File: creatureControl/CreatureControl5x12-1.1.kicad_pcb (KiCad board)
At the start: 2 copper layers, 120 x 50 mm, 42 parts, among them J1 USB_C_Receptacle_GCT_USB4125-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, J2 BarrelJack_Horizontal, J3 TerminalBlock_4Ucon_1x02_P3.5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

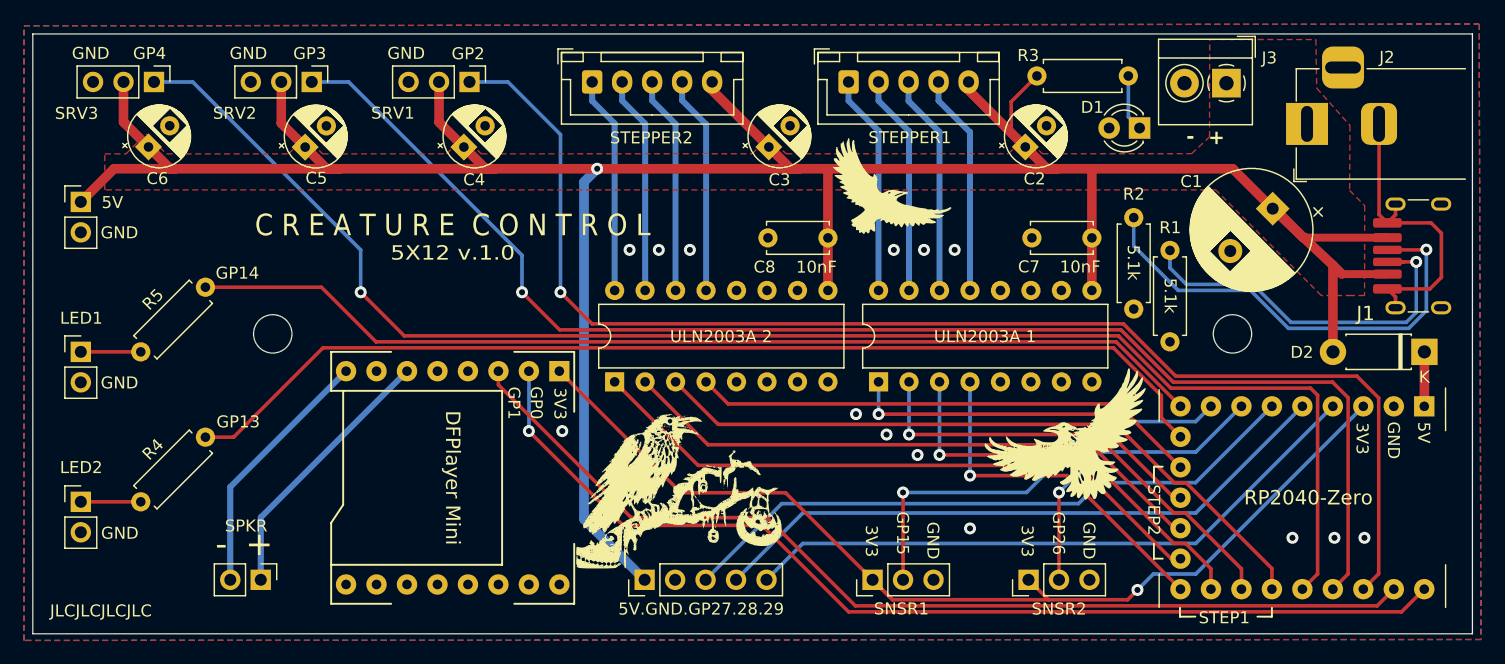
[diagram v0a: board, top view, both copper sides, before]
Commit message: Update CC5x12 to v1.1
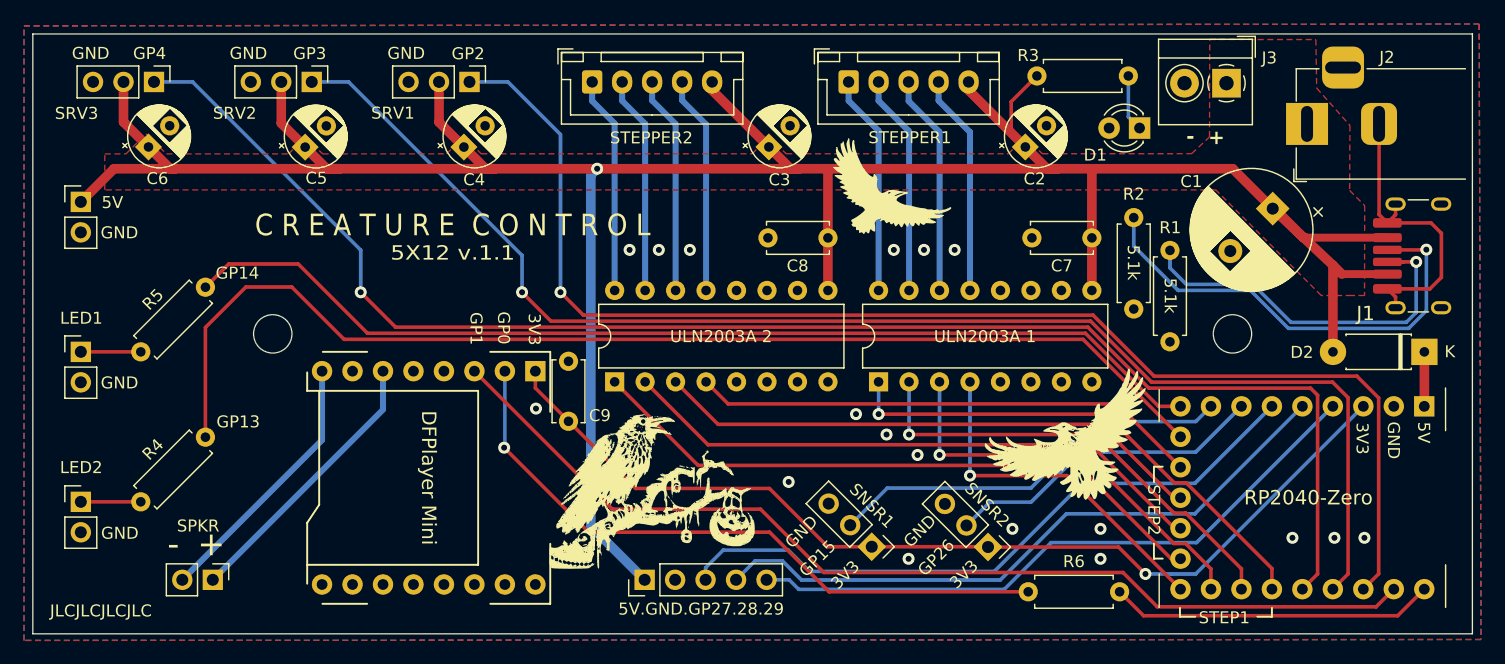
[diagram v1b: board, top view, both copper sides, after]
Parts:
- added C9: C_Disc_D5.0mm_W2.5mm_P5.00mm, Capacitor_THT:C_Disc_D5.0mm_W2.5mm_P5.00mm, F.Cu at (124.7, 62.3)
- added R6: 5.1 kΩ, Resistor_THT:R_Axial_DIN0207_L6.3mm_D2.5mm_P7.62mm_Horizontal, F.Cu at (170.6, 76.5)
- moved SNSR2 4.35 mm to (159.6, 72.8), turned to -135 degrees
- moved SPKR 4.00 mm to (95.0, 75.5)
- moved SNSR1 2.76 mm to (149.9, 72.7), turned to -135 degrees
- moved G*** 2.24 mm to (131.8, 67.1)
- moved DFPlayer Mini 2.00 mm to (113.0, 67.0)
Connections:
- DFPlayer Mini pad 2: GP0 -> DFRX
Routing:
- net GP0: track 86.7 -> 27.1 mm, vias 1 -> 0
- net DFRX: track 0.00 -> 55.1 mm, vias 0 -> 1
- net GP13: track 88.5 -> 97.0 mm
- net 3V3: track 86.3 -> 82.6 mm
- net GP27: track 53.2 -> 55.3 mm
- net GP15: track 35.9 -> 34.2 mm, vias 1 -> 0
- net GP14: track 85.4 -> 87.0 mm
- net GP26: track 25.5 -> 27.0 mm, vias 1 -> 0
- net 5V: track 247.0 -> 245.5 mm
- net GP1: track 84.0 -> 85.4 mm
- net GP28: track 53.2 -> 54.5 mm
- net SPKR-: track 21.4 -> 22.2 mm
- net SPKR+: track 22.4 -> 23.3 mm
- net GP29: track 53.2 -> 53.9 mm
- net GP11: track 46.1 -> 45.5 mm
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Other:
- board text added: "5X12 v.1.1"
- board text added: "github.com/swaziloo/halloween"
- board text removed: "10nF"
- board text removed: "5X12 v.1.0"
- board text removed: "monkeymind.com/halloween"
